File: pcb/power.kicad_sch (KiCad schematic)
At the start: 68 parts, among them Q1 NFET_250V_10A_TPH1110FNH,L1Q, U5 REG_SW_BOOST_TI_TLV61046ADBV, U6 REG_SW_BOOST_TI_LM51561HPWPR, U7 REG_LDO_3V3_250mA_TI_LP5907MF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

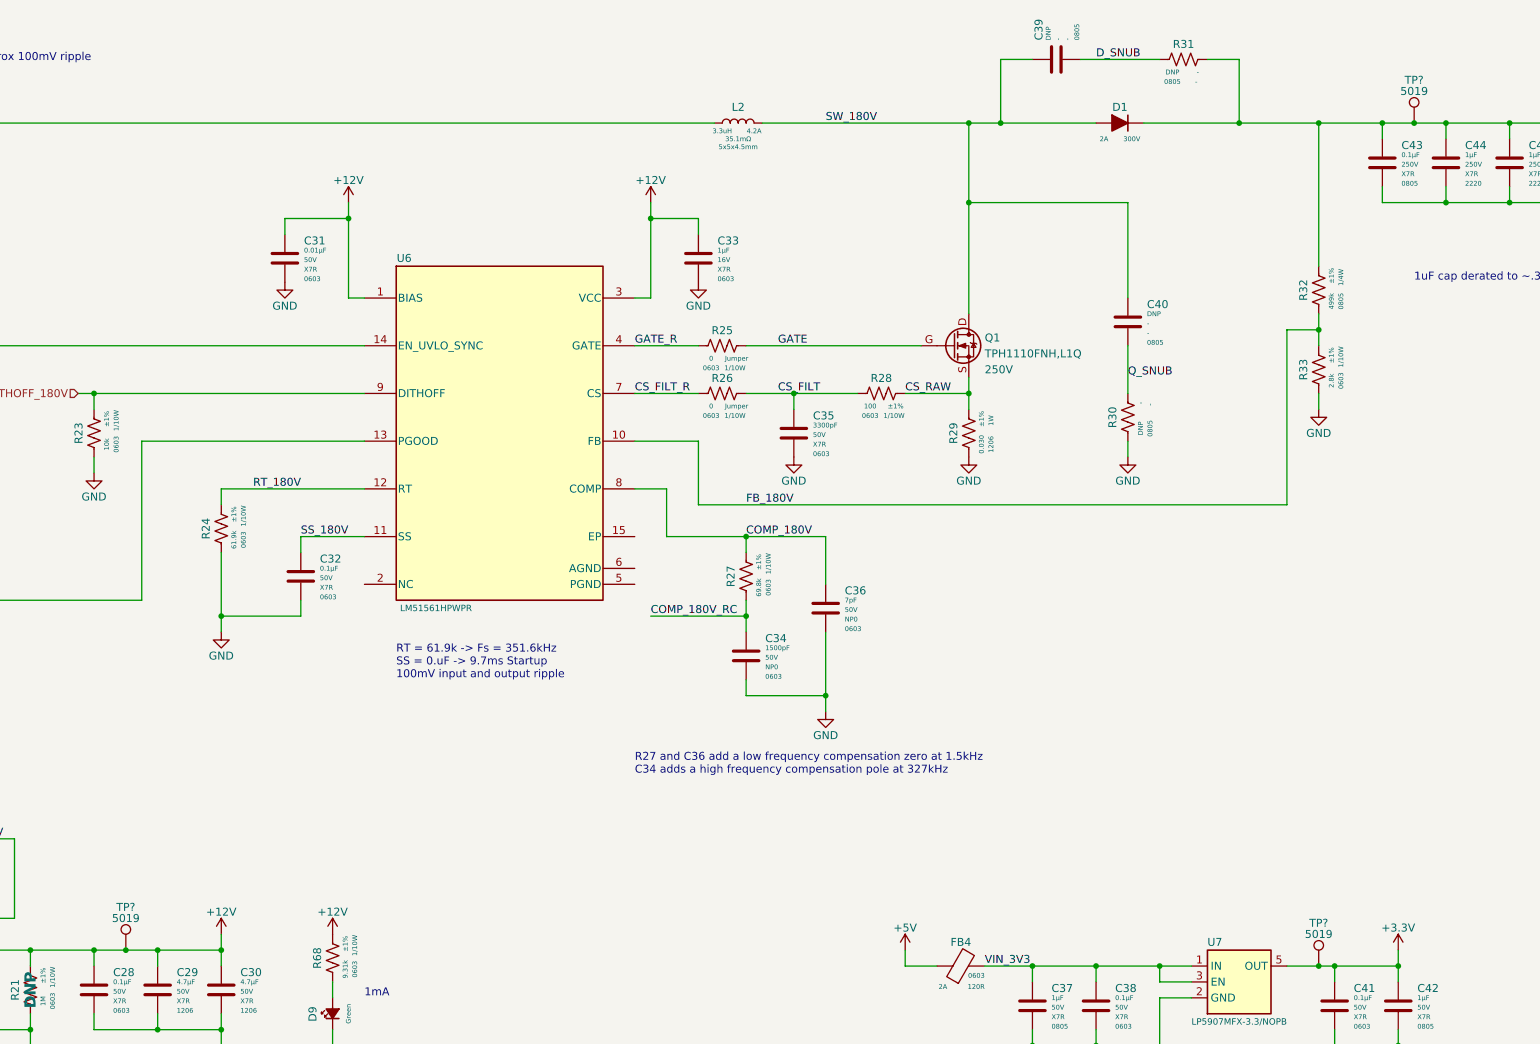
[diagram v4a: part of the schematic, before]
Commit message: Fixed a bunch of footprints and added missing 3D models
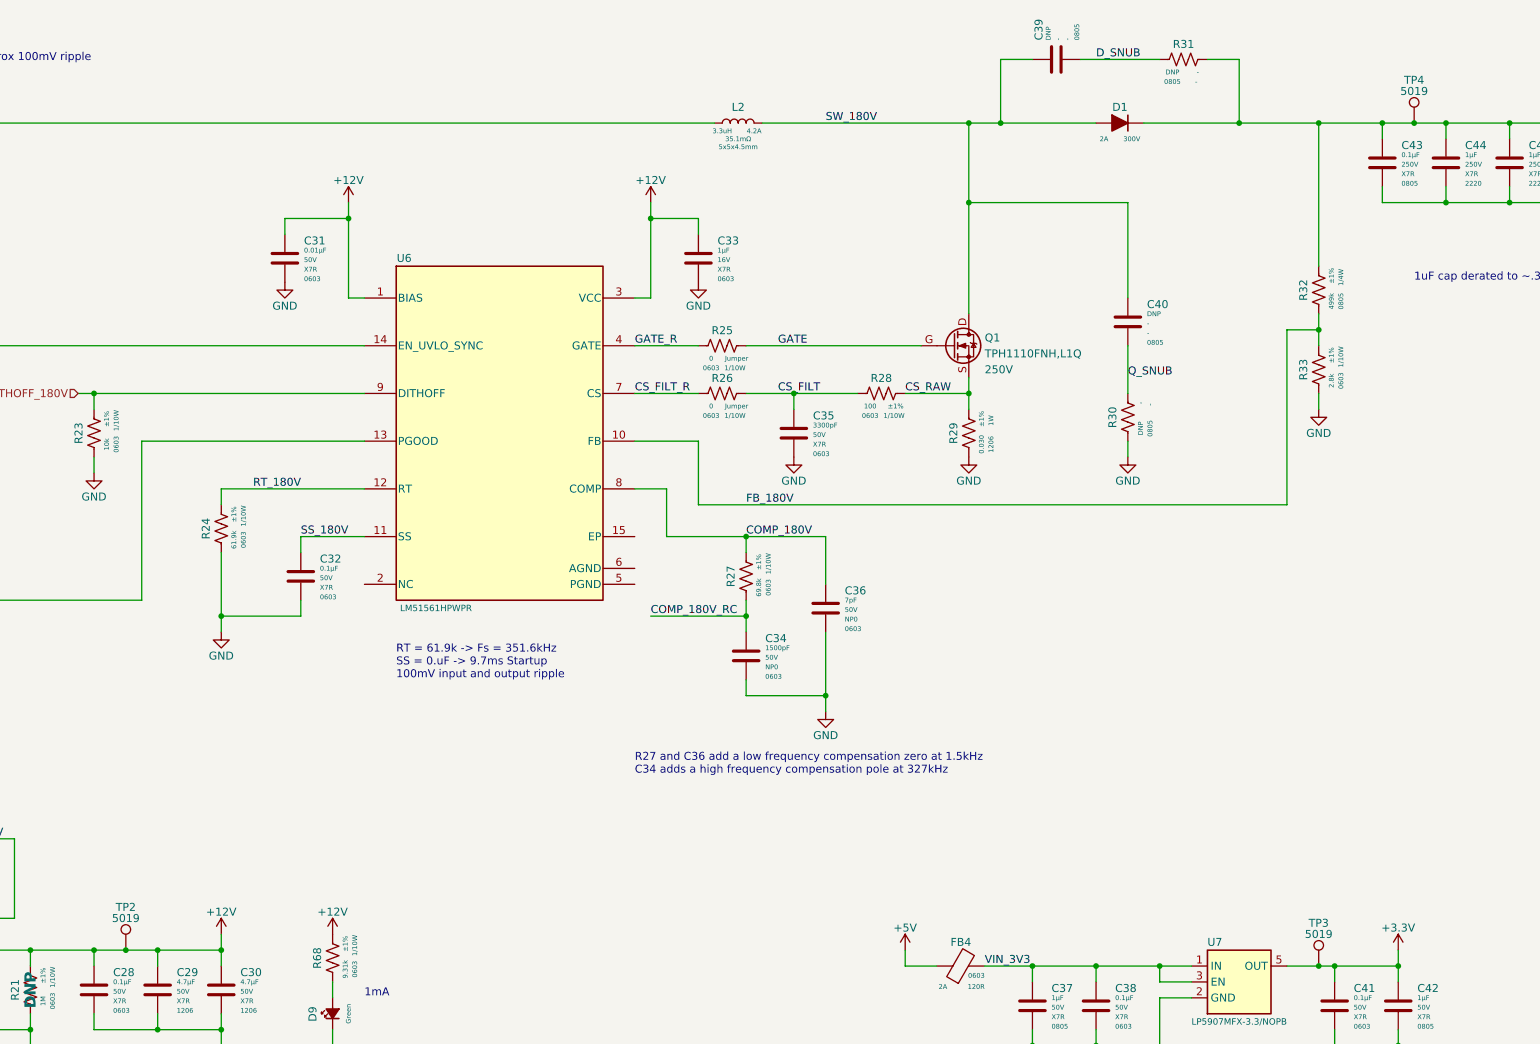
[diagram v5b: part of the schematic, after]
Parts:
- gave numbers to parts that had none: 3
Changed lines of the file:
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@@
   (symbol (lib_id ".arjun:TP_KEYSTONE_5019") (at 340.36 35.56 0) (unit 1)
     (in_bom yes) (on_board yes)
-    (property "Reference" "TP?" (id 0) (at 340.36 28.702 0))
+    (property "Reference" "TP4" (id 0) (at 340.36 28.702 0))
     (property "Value" "TP_KEYSTONE_5019" (id 1) (at 354.33 22.86 0)
       (effects (font (size 1.27 1.27)) (justify left) hide)
@@
   (symbol (lib_id ".arjun:TP_KEYSTONE_5019") (at 134.62 167.64 0) (unit 1)
     (in_bom yes) (on_board yes)
-    (property "Reference" "TP?" (id 0) (at 134.62 160.782 0))
+    (property "Reference" "TP2" (id 0) (at 134.62 160.782 0))
     (property "Value" "TP_KEYSTONE_5019" (id 1) (at 148.59 154.94 0)
       (effects (font (size 1.27 1.27)) (justify left) hide)
@@
   (symbol (lib_id ".arjun:TP_KEYSTONE_5019") (at 325.12 170.18 0) (unit 1)
     (in_bom yes) (on_board yes)
-    (property "Reference" "TP?" (id 0) (at 325.12 163.322 0))
+    (property "Reference" "TP3" (id 0) (at 325.12 163.322 0))
     (property "Value" "TP_KEYSTONE_5019" (id 1) (at 339.09 157.48 0)
       (effects (font (size 1.27 1.27)) (justify left) hide)
@@
     (pin "1")
   )
-  (symbol (lib_id ".arjun:RES_DNP_0805") (at 294.64 78.74 0) (unit 1)
+  (symbol (lib_name "RES_DNP_0805_1") (lib_id ".arjun:RES_DNP_0805") (at 294.64 78.74 0) (unit 1)
     (in_bom yes) (on_board yes)
     (property "Reference" "R30" (id 0) (at 291.465 82.55 90)

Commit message: Started layout!! 180V boost mostly laid out
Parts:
- C39, C40, R30, R31: now not fitted
- R17, R19, R20, R23: symbol .arjun:RES_10K_1P_1/10W_0603 -> .arjun:RES_10K_1P_1/10W_0603
- R18, R25, R26: symbol .arjun:RES_0R_1/10W_0603 -> .arjun:RES_0R_1/10W_0603
- R21: symbol .arjun:RES_1M_1P_1/10W_0603 -> .arjun:RES_1M_1P_1/10W_0603; now not fitted; now in the parts list
- R22: symbol .arjun:RES_71K5_1P_1/10W_0603 -> .arjun:RES_71K5_1P_1/10W_0603; now not fitted; now in the parts list
- R24: symbol .arjun:RES_61K9_1P_1/10W_0603 -> .arjun:RES_61K9_1P_1/10W_0603
- R27: symbol .arjun:RES_69K8_1P_1/10W_0603 -> .arjun:RES_69K8_1P_1/10W_0603
- R28: symbol .arjun:RES_100R_1P_1/10W_0603 -> .arjun:RES_100R_1P_1/10W_0603
- R32, R45: symbol .arjun:RES_499K_1P_1/4W_0805 -> .arjun:RES_499K_1P_1/4W_0805
- R33: symbol .arjun:RES_2K8_1P_1/10W_0603 -> .arjun:RES_2K8_1P_1/10W_0603
- R43: symbol .arjun:RES_33K_1P_1/10W_0603 -> .arjun:RES_33K_1P_1/10W_0603
- R44, R46: symbol .arjun:RES_4K7_1P_1/10W_0603 -> .arjun:RES_4K7_1P_1/10W_0603
- R67: symbol .arjun:RES_1K5_1P_1/10W_0603 -> .arjun:RES_1K5_1P_1/10W_0603
- R68: symbol .arjun:RES_9K31_1P_1/10W_0603 -> .arjun:RES_9K31_1P_1/10W_0603
- R69: symbol .arjun:RES_698R_1P_1/10W_0603 -> .arjun:RES_698R_1P_1/10W_0603
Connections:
- net GND: now also U6.15 (EP), U6.5 (PGND), U6.6 (AGND)
- no-connect marks 0 -> 1
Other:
- note added: "Add PG Pull up at MCU pin"
- moved on the sheet: C34, C36, R27

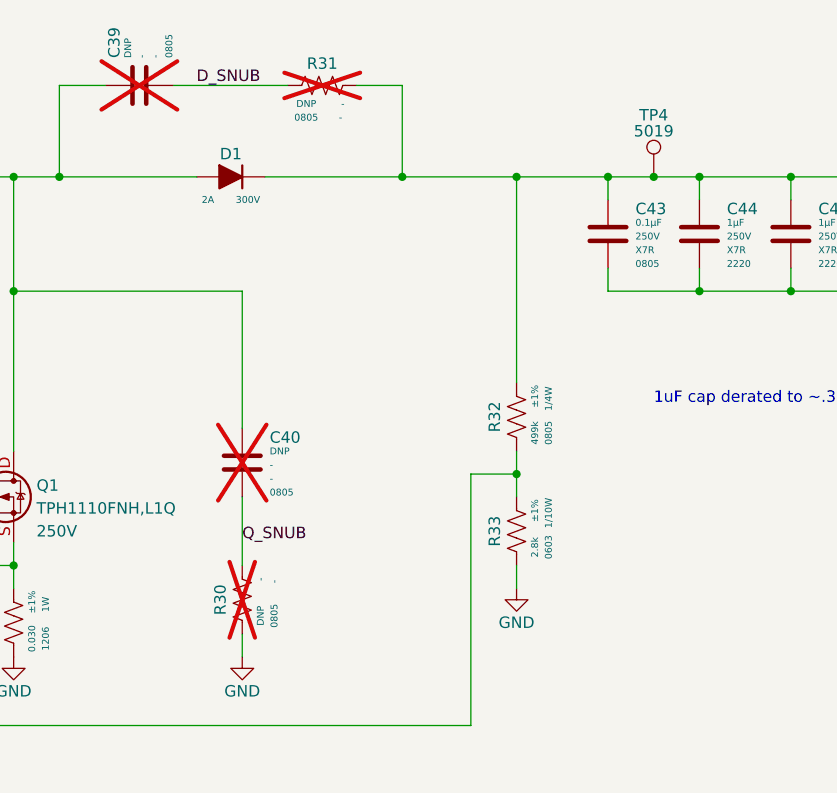
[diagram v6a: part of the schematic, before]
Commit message: Added 180V clearance rules. Updated 0805 footprints to 1206 for 180V nets.
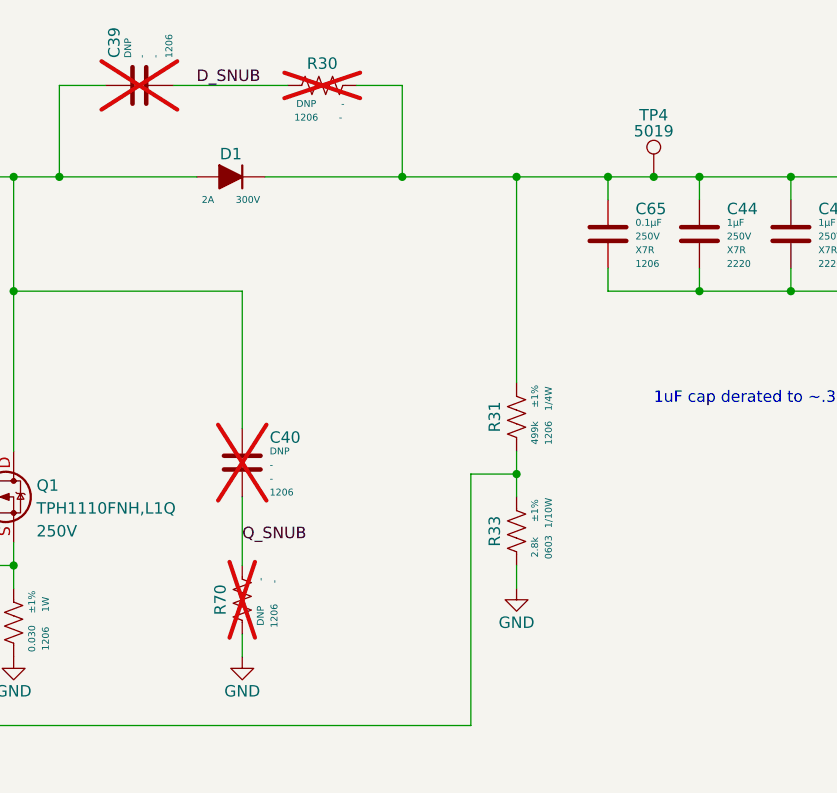
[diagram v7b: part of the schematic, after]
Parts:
- removed C39, C40: CAP_CER_DNP_0805, Capacitor_SMD:C_0805_2012Metric, symbol .arjun:CAP_CER_DNP_0805
- removed C43: CAP_CER_0u1_250V_X7R_0805, Capacitor_SMD:C_0805_2012Metric, symbol .arjun:CAP_CER_0u1_250V_X7R_0805
- removed R30, R31: RES_DNP_0805, Resistor_SMD:R_0805_2012Metric, symbol .arjun:RES_DNP_0805
- removed R32: RES_499K_1P_1/4W_0805, Resistor_SMD:R_0805_2012Metric, symbol .arjun:RES_499K_1P_1/4W_0805
- added C39, C40: CAP_CER_DNP_1206, Capacitor_SMD:C_1206_3216Metric, symbol arjun_lib:CAP_CER_DNP_1206
- added C65: CAP_CER_0u1_250V_X7R_1206, Capacitor_SMD:C_1206_3216Metric, symbol arjun_lib:CAP_CER_0u1_250V_X7R_1206
- added R30, R70: RES_DNP_1206, Resistor_SMD:R_1206_3216Metric, symbol arjun_lib:RES_DNP_1206
- added R31: RES_499K_1P_1/4W_1206, Resistor_SMD:R_1206_3216Metric, symbol arjun_lib:RES_499K_1P_1/4W_1206
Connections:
- net 180V: now also C65.1, R30.1, R31.1
- net D_SNUB: now also C39.2, R30.2
- net FB_180V: now also R31.2
- net GND: now also C65.2, R70.2
- net Q_SNUB: now also C40.2, R70.1
- net SW_180V: now also C39.1, C40.1

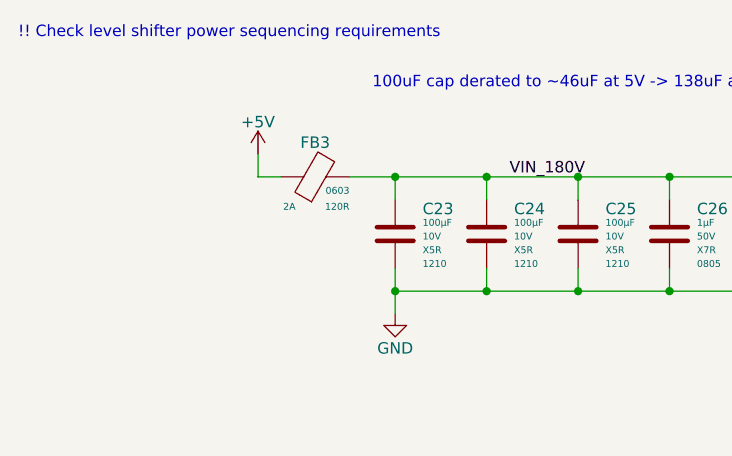
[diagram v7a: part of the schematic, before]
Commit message: Added note about mcu reset
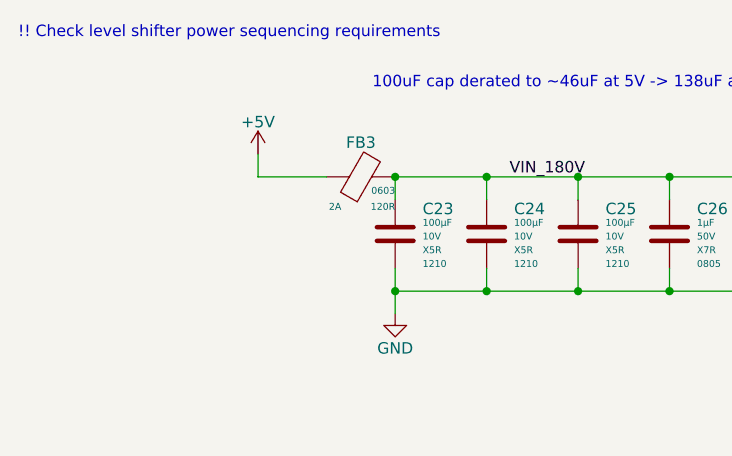
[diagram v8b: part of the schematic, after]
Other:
- moved on the sheet: FB3
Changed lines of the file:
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@@
 	(wire
 		(pts
-			(xy 58.42 35.56) (xy 63.5 35.56)
-		)
-		(stroke
-			(width 0)
-			(type default)
-		)
-	)
-	(wire
-		(pts
 			(xy 215.9 86.36) (xy 229.87 86.36)
 		)
@@
 	(wire
 		(pts
-			(xy 48.26 35.56) (xy 50.8 35.56)
+			(xy 48.26 35.56) (xy 55.88 35.56)
 		)
 		(stroke
@@
 	(symbol
 		(lib_id ".arjun:FER_120R_2A_0603")
-		(at 50.8 35.56 0)
+		(at 55.88 35.56 0)
 		(unit 1)
 		(exclude_from_sim no)
@@
 		(dnp no)
 		(property "Reference" "FB3"
-			(at 54.61 31.75 0)
+			(at 59.69 31.75 0)
 			(effects
 				(font
@@
 		)
 		(property "Value" "FER_120R_2A_0603"
-			(at 80.645 29.21 0)
+			(at 85.725 29.21 0)
 			(effects
 				(font
@@
 		)
 		(property "Footprint" "Inductor_SMD:L_0603_1608Metric"
-			(at 78.994 26.67 0)
+			(at 84.074 26.67 0)
 			(effects
 				(font
@@
 		)
 		(property "Datasheet" "https://www.murata.com/en-us/products/productdetail?partno=BLM18PG121SH1%23"
-			(at 108.585 41.91 0)
+			(at 113.665 41.91 0)
 			(effects
 				(font
@@
 		)
 		(property "Description" ""
-			(at 50.8 35.56 0)
+			(at 55.88 35.56 0)
 			(effects
 				(font
@@
 		)
 		(property "Manufacturer" "Murata Electronics"
-			(at 70.485 31.75 0)
+			(at 75.565 31.75 0)
 			(effects
 				(font
@@
 		)
 		(property "ManufacturerPN" "BLM18PG121SH1D"
-			(at 70.485 34.29 0)
+			(at 75.565 34.29 0)
 			(effects
 				(font
@@
 		)
 		(property "Vendor" "Digi-Key"
-			(at 70.485 36.83 0)
+			(at 75.565 36.83 0)
 			(effects
 				(font
@@
 		)
 		(property "VendorPN" "490-7815-1-ND"
-			(at 70.485 39.37 0)
+			(at 75.565 39.37 0)
 			(effects
 				(font
@@
 		)
 		(property "Impedance@100MHz" "120R"
-			(at 58.42 38.862 0)
+			(at 63.5 38.862 0)
 			(effects
 				(font
@@
 		)
 		(property "Rated Current" "2A"
-			(at 51.054 38.862 0)
+			(at 56.134 38.862 0)
 			(effects
 				(font
@@
 		)
 		(property "Package" "0603"
-			(at 58.42 37.084 0)
+			(at 63.5 37.084 0)
 			(effects
 				(font
